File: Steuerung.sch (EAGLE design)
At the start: 3 parts

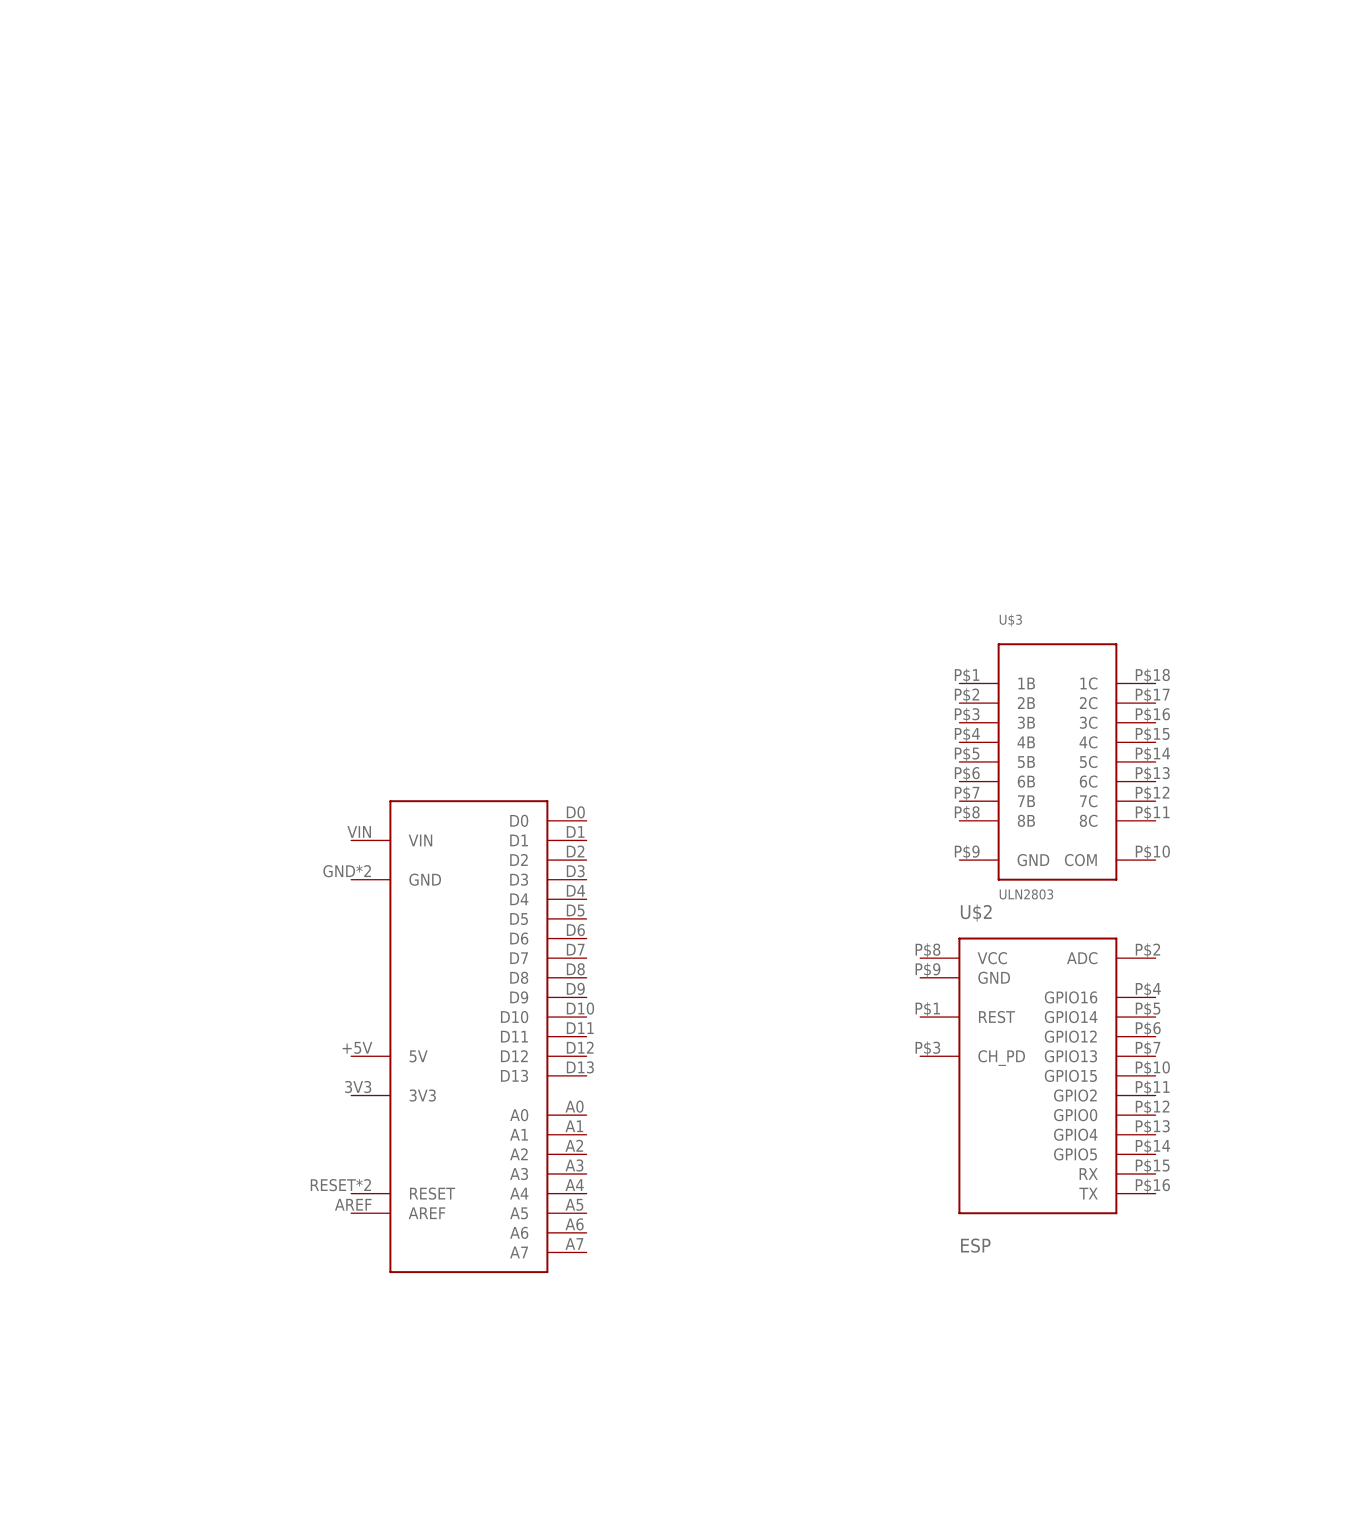
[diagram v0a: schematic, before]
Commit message: Schaltplan für 16MHz/5V Nano und ESP-Witty adaptiert
Signed-off-by: Wolfgang Kraft <fablab-ka@wkraft.org>
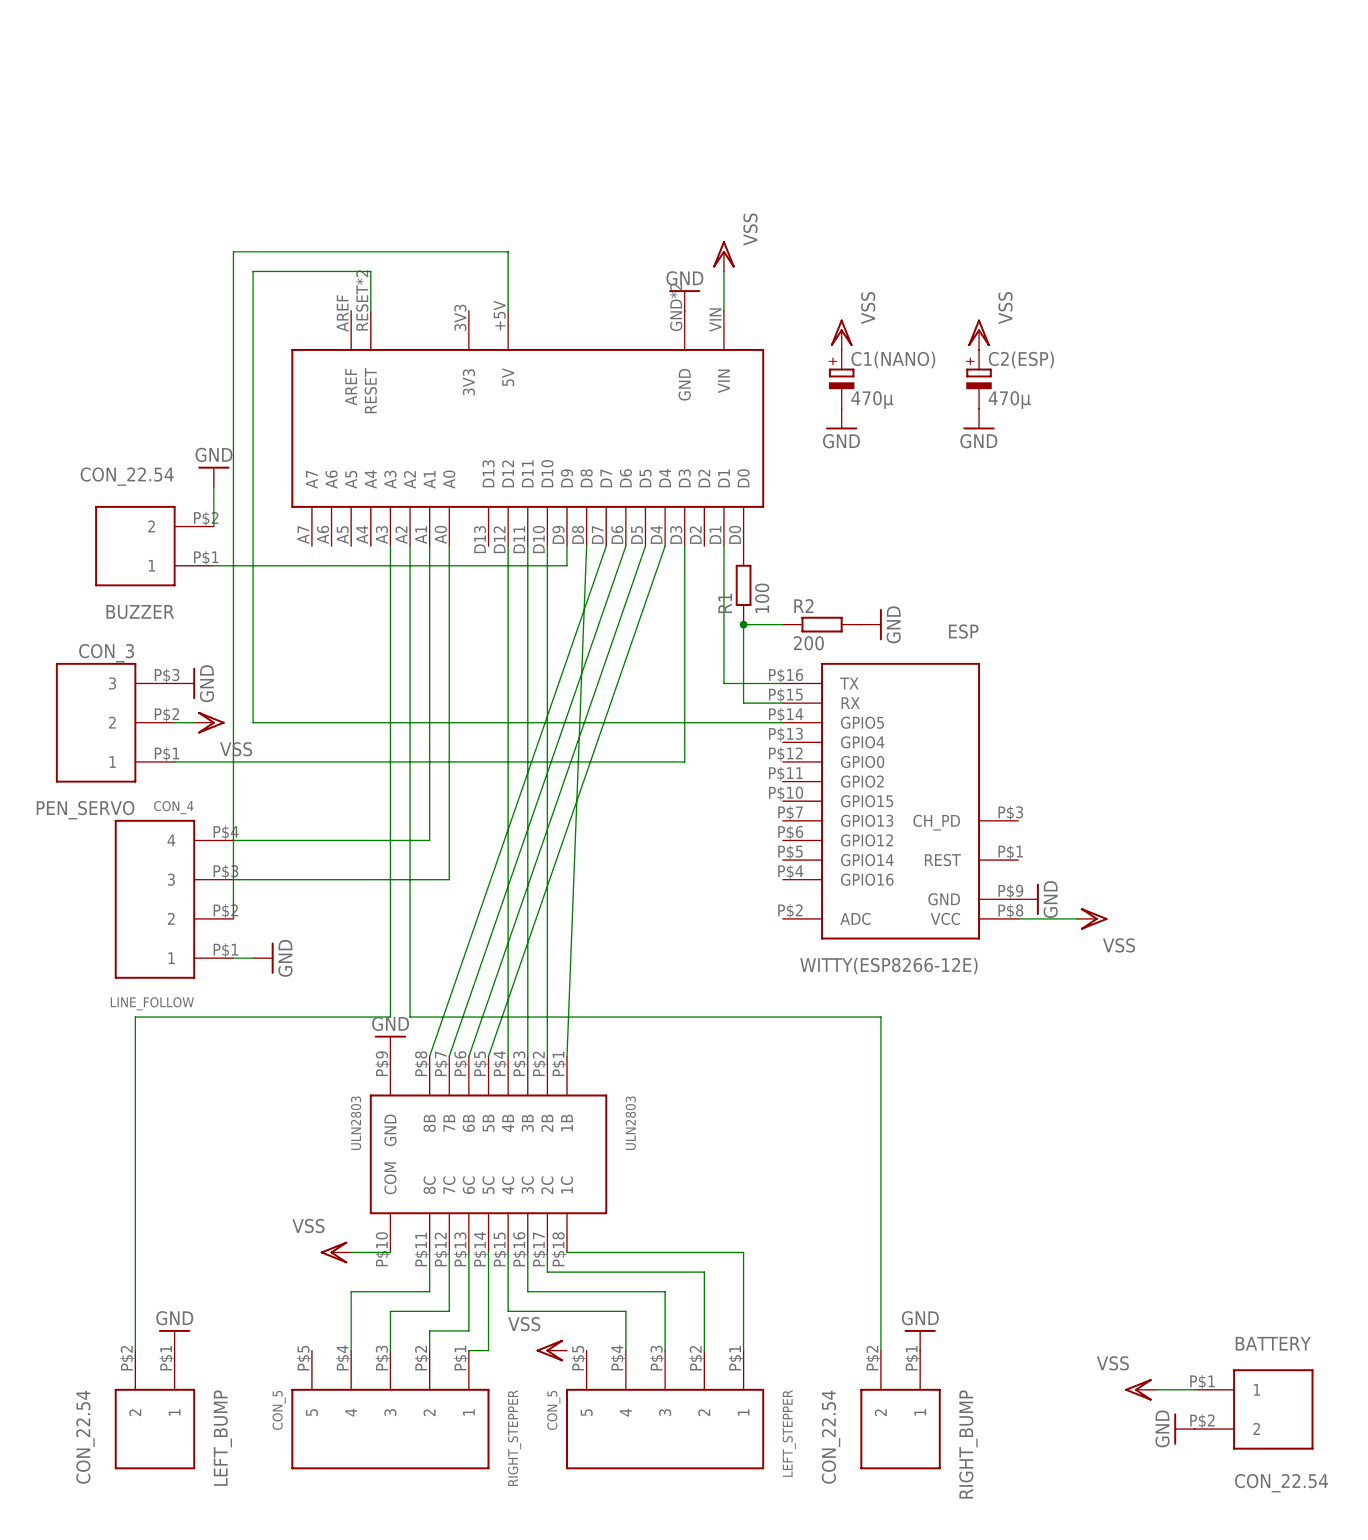
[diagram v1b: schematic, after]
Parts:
- removed U$1: ARDUINO_NANO, pcaroli:ARDUINO_NANO
- removed U$2: ESP, pcaroli:ESP
- removed U$3: ULN2803, pcaroli:ULN2803
- added ARDUINO_NANO: ARDUINO_NANO, pcaroli:ARDUINO_NANO
- added BATTERY, BUZZER, LEFT_BUMP, RIGHT_BUMP: CON_22.54, pcaroli:CON_22.54
- added C1(NANO), C2(ESP): 470µ, resistor:CPOL-EUE2.5-7
- added LEFT_STEPPER, RIGHT_STEPPER: CON_5, pcaroli:CON_5
- added LINE_FOLLOW: CON_4, pcaroli:CON_4
- added PEN_SERVO: CON_3, pcaroli:CON_3
- added R1: 100, resistor:R-EU_0204/7
- added R2: 200, resistor:R-EU_0204/7
- added ULN2803: ULN2803, pcaroli:ULN2803
- added WITTY(ESP8266-12E): ESP, pcaroli:ESP
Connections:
- new net GND: ARDUINO_NANO.GND, BATTERY.2, BUZZER.2, C1(NANO).-, C2(ESP).-, LEFT_BUMP.1, LINE_FOLLOW.1, PEN_SERVO.3, R2.2, RIGHT_BUMP.1, ULN2803.GND, WITTY(ESP8266-12E).GND
- new net N$1: LEFT_STEPPER.1, ULN2803.1C
- new net N$10: ARDUINO_NANO.D10, ULN2803.2B
- new net N$11: ARDUINO_NANO.D11, ULN2803.3B
- new net N$12: ARDUINO_NANO.D12, ULN2803.4B
- new net N$13: ARDUINO_NANO.D4, ULN2803.5B
- new net N$14: ARDUINO_NANO.D5, ULN2803.6B
- new net N$15: ARDUINO_NANO.D6, ULN2803.7B
- new net N$16: ARDUINO_NANO.D7, ULN2803.8B
- new net N$17: ARDUINO_NANO.A3, LEFT_BUMP.2
- new net N$18: ARDUINO_NANO.A2, RIGHT_BUMP.2
- new net N$19: ARDUINO_NANO.D0, R1.2
- new net N$2: LEFT_STEPPER.2, ULN2803.2C
- new net N$20: R1.1, R2.1, WITTY(ESP8266-12E).RX
- new net N$21: ARDUINO_NANO.D1, WITTY(ESP8266-12E).TX
- new net N$22: ARDUINO_NANO.RESET, WITTY(ESP8266-12E).GPIO5
- new net N$23: ARDUINO_NANO.D9, BUZZER.1
- new net N$24: ARDUINO_NANO.D3, PEN_SERVO.1
- new net N$25: ARDUINO_NANO.A1, LINE_FOLLOW.4
- new net N$26: ARDUINO_NANO.A0, LINE_FOLLOW.3
- new net N$27: ARDUINO_NANO.5V, LINE_FOLLOW.2
- new net N$3: LEFT_STEPPER.3, ULN2803.3C
- new net N$4: LEFT_STEPPER.4, ULN2803.4C
- new net N$5: RIGHT_STEPPER.1, ULN2803.5C
- new net N$6: RIGHT_STEPPER.2, ULN2803.6C
- new net N$7: RIGHT_STEPPER.3, ULN2803.7C
- new net N$8: RIGHT_STEPPER.4, ULN2803.8C
- new net N$9: ARDUINO_NANO.D8, ULN2803.1B
- new net VSS: ARDUINO_NANO.VIN, BATTERY.1, C1(NANO).+, C2(ESP).+, PEN_SERVO.2, ULN2803.COM, WITTY(ESP8266-12E).VCC

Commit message: minor correction
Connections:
- net VSS: now also LEFT_STEPPER.5, RIGHT_STEPPER.5
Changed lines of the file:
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@@
 <setting verticaltext="up"/>
 </settings>
-<grid distance="0.1" unitdist="inch" unit="inch" style="lines" multiple="1" display="yes" altdistance="0.01" altunitdist="inch" altunit="inch"/>
+<grid distance="0.1" unitdist="inch" unit="inch" style="lines" multiple="1" display="no" altdistance="0.01" altunitdist="inch" altunit="inch"/>
 <layers>
 <layer number="1" name="Top" color="4" fill="1" visible="no" active="no"/>
@@
 <part name="GND11" library="supply1" deviceset="GND" device=""/>
 <part name="GND12" library="supply1" deviceset="GND" device=""/>
+<part name="VSS9" library="supply1" deviceset="VSS" device=""/>
 </parts>
 <sheets>
@@
 <instance part="GND11" gate="1" x="83.82" y="121.92"/>
 <instance part="GND12" gate="1" x="66.04" y="121.92"/>
+<instance part="VSS9" gate="G$1" x="-10.16" y="2.54" rot="R270"/>
 </instances>
 <busses>
@@
 <pinref part="VSS7" gate="G$1" pin="VSS"/>
 </segment>
-</net>
+<segment>
+<pinref part="RIGHT_STEPPER" gate="G$1" pin="5"/>
+<pinref part="VSS9" gate="G$1" pin="VSS"/>
+<wire x1="-7.62" y1="2.54" x2="-2.54" y2="2.54" width="0.1524" layer="91"/>
+</segment>
+<segment>
+<pinref part="LEFT_STEPPER" gate="G$1" pin="5"/>
+<pinref part="VSS5" gate="G$1" pin="VSS"/>
+<wire x1="30.48" y1="2.54" x2="33.02" y2="2.54" width="0.1524" layer="91"/>
+</segment>
+</net>

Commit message: First PCB
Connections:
- net N$1: now also LEFT_STEPPER.4; no longer LEFT_STEPPER.1
- net N$10: now also ULN2803.3B; no longer ULN2803.2B
- net N$11: now also ULN2803.2B; no longer ULN2803.3B
- net N$12: now also ULN2803.1B; no longer ULN2803.4B
- net N$13: now also ARDUINO_NANO.D7; no longer ARDUINO_NANO.D4
- net N$14: now also ARDUINO_NANO.D6; no longer ARDUINO_NANO.D5
- net N$15: now also ARDUINO_NANO.D5; no longer ARDUINO_NANO.D6
- net N$16: now also ARDUINO_NANO.D4; no longer ARDUINO_NANO.D7
- net N$2: now also LEFT_STEPPER.3; no longer LEFT_STEPPER.2
- net N$3: now also LEFT_STEPPER.2; no longer LEFT_STEPPER.3
- net N$4: now also LEFT_STEPPER.1; no longer LEFT_STEPPER.4
- net N$5: now also RIGHT_STEPPER.4; no longer RIGHT_STEPPER.1
- net N$6: now also RIGHT_STEPPER.3; no longer RIGHT_STEPPER.2
- net N$7: now also RIGHT_STEPPER.2; no longer RIGHT_STEPPER.3
- net N$8: now also RIGHT_STEPPER.1; no longer RIGHT_STEPPER.4
- net N$9: now also ULN2803.4B; no longer ULN2803.1B
